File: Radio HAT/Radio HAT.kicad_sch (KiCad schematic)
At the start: 21 parts, among them J1 Raspberry_Pi_2_3, J2 Coax SMA, J3 Barrel_Jack, J4 VCC, J5 6V, J6 GND, U1 RFM98PW, U2 AZ2185D-ADJTRG1

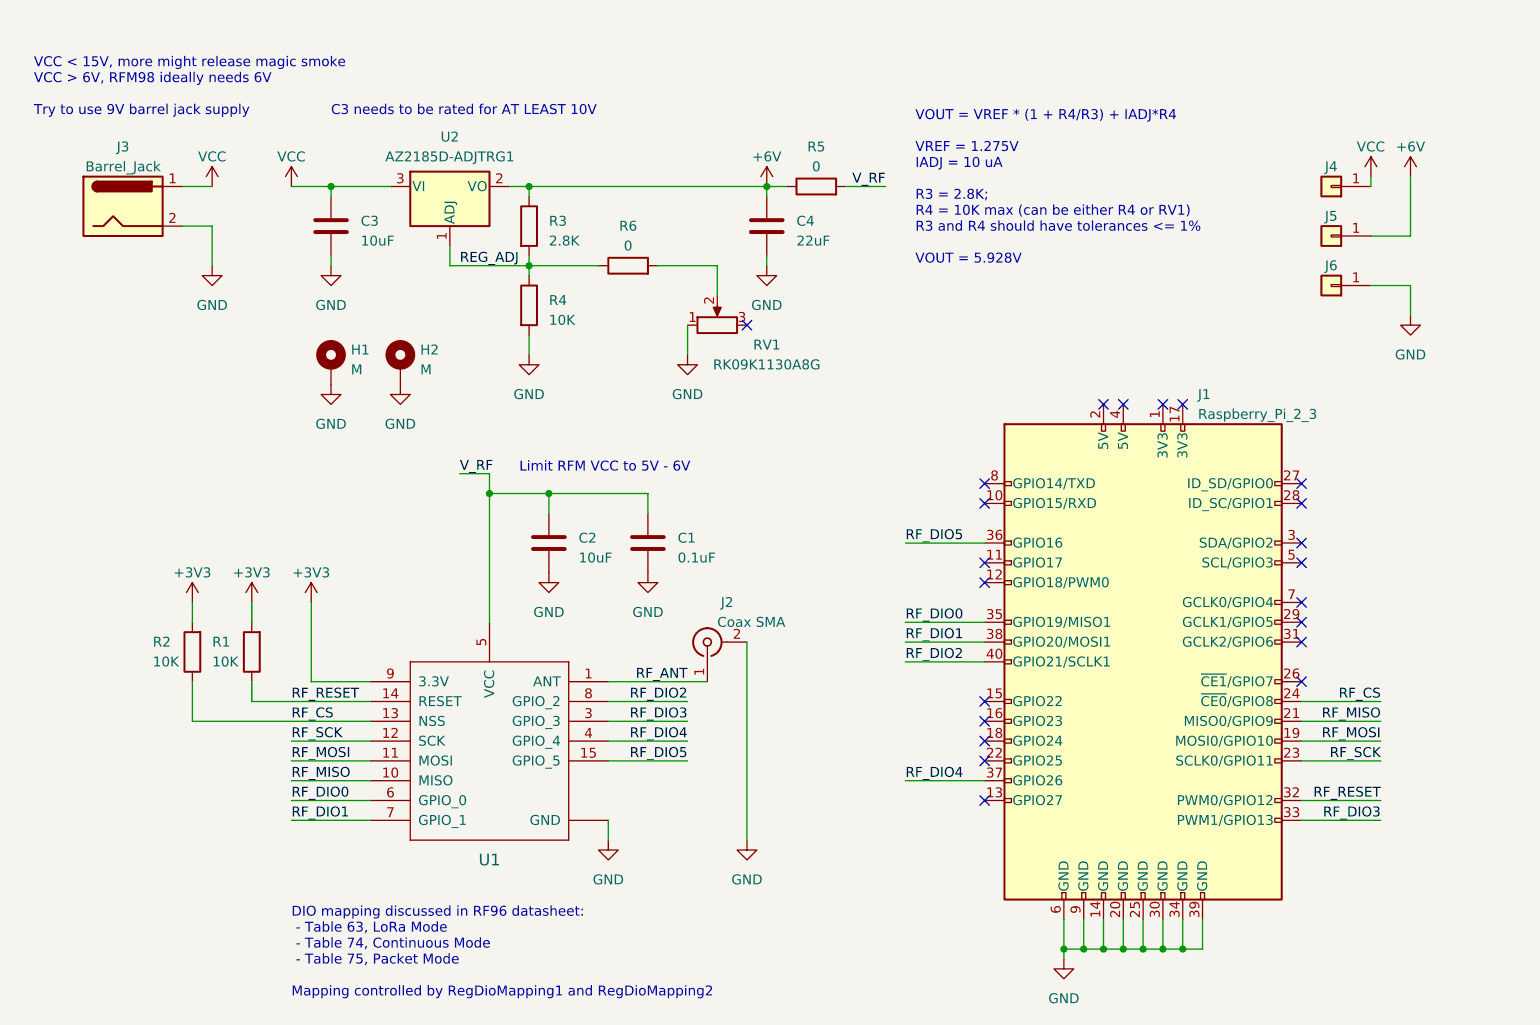
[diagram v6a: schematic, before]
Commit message: Updated schematic, changed power routing
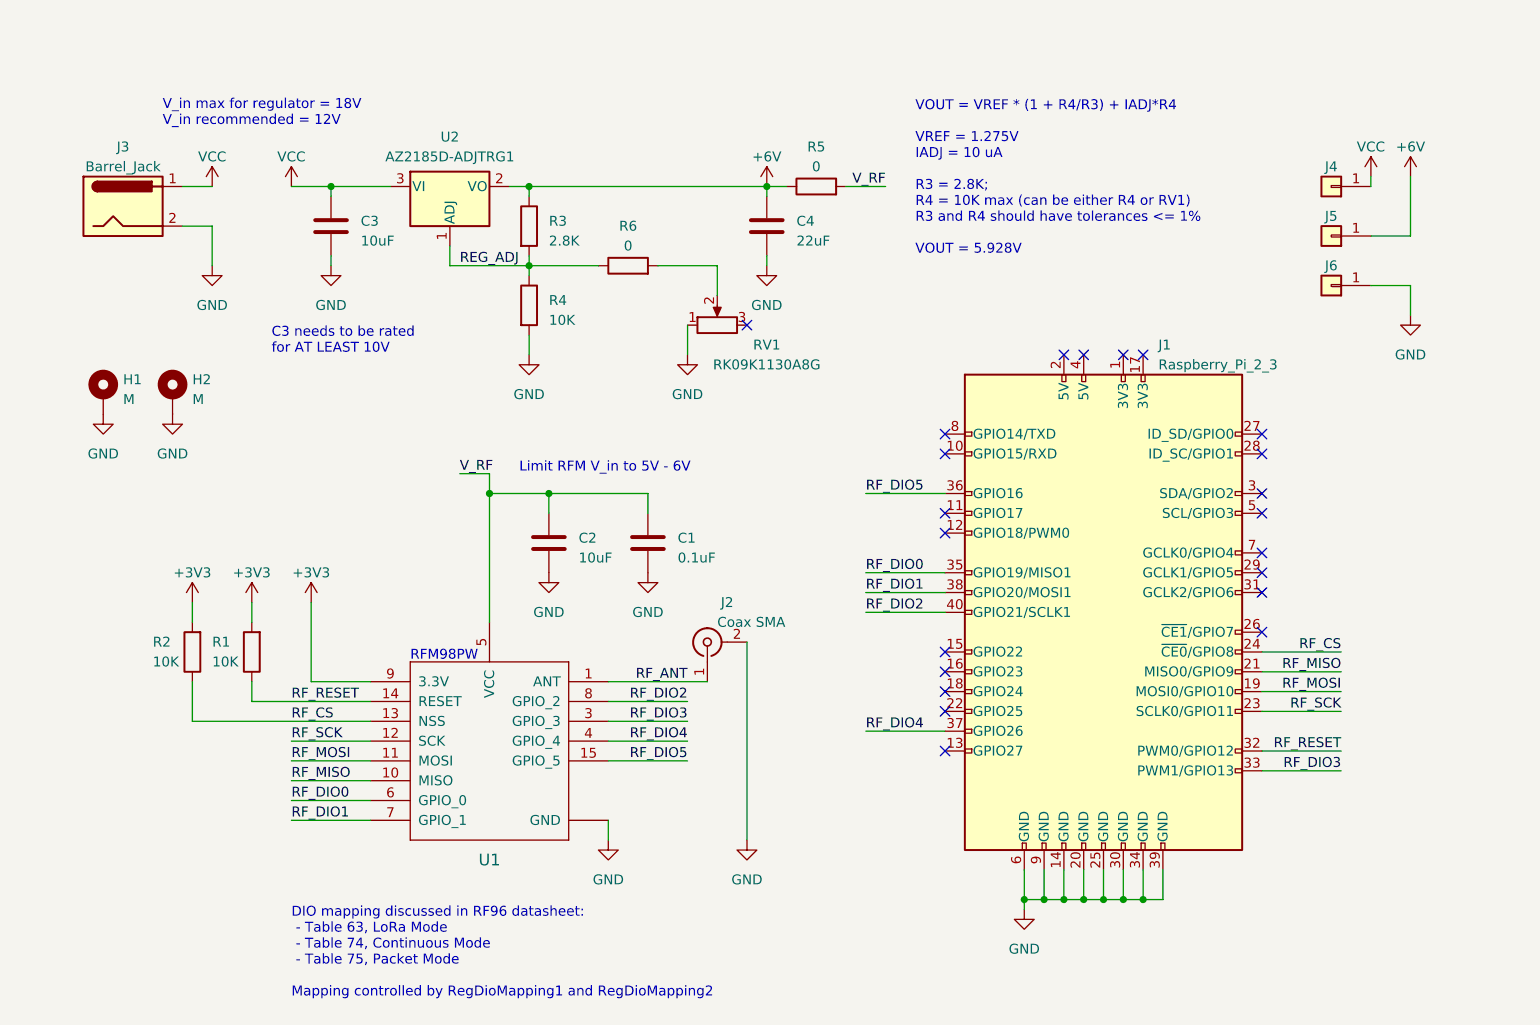
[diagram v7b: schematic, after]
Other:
- note added: "Limit RFM V_in to 5V - 6V"
- note added: "RFM98PW"
- note added: "V_in max for regulator = 18V V_in recommended = 12V"
- note removed: "Limit RFM VCC to 5V - 6V"
- note removed: "VCC < 15V, more might release magic smoke VCC > 6V, RFM98 ideally needs 6V Try to use 9V barrel jack supply"
- moved on the sheet: H1, H2, J1

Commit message: Reworked power traces, added stitching vias
Reworked 3V3 net, added stitching vias on board, added passive components, regenerated BOM and STEP file for board
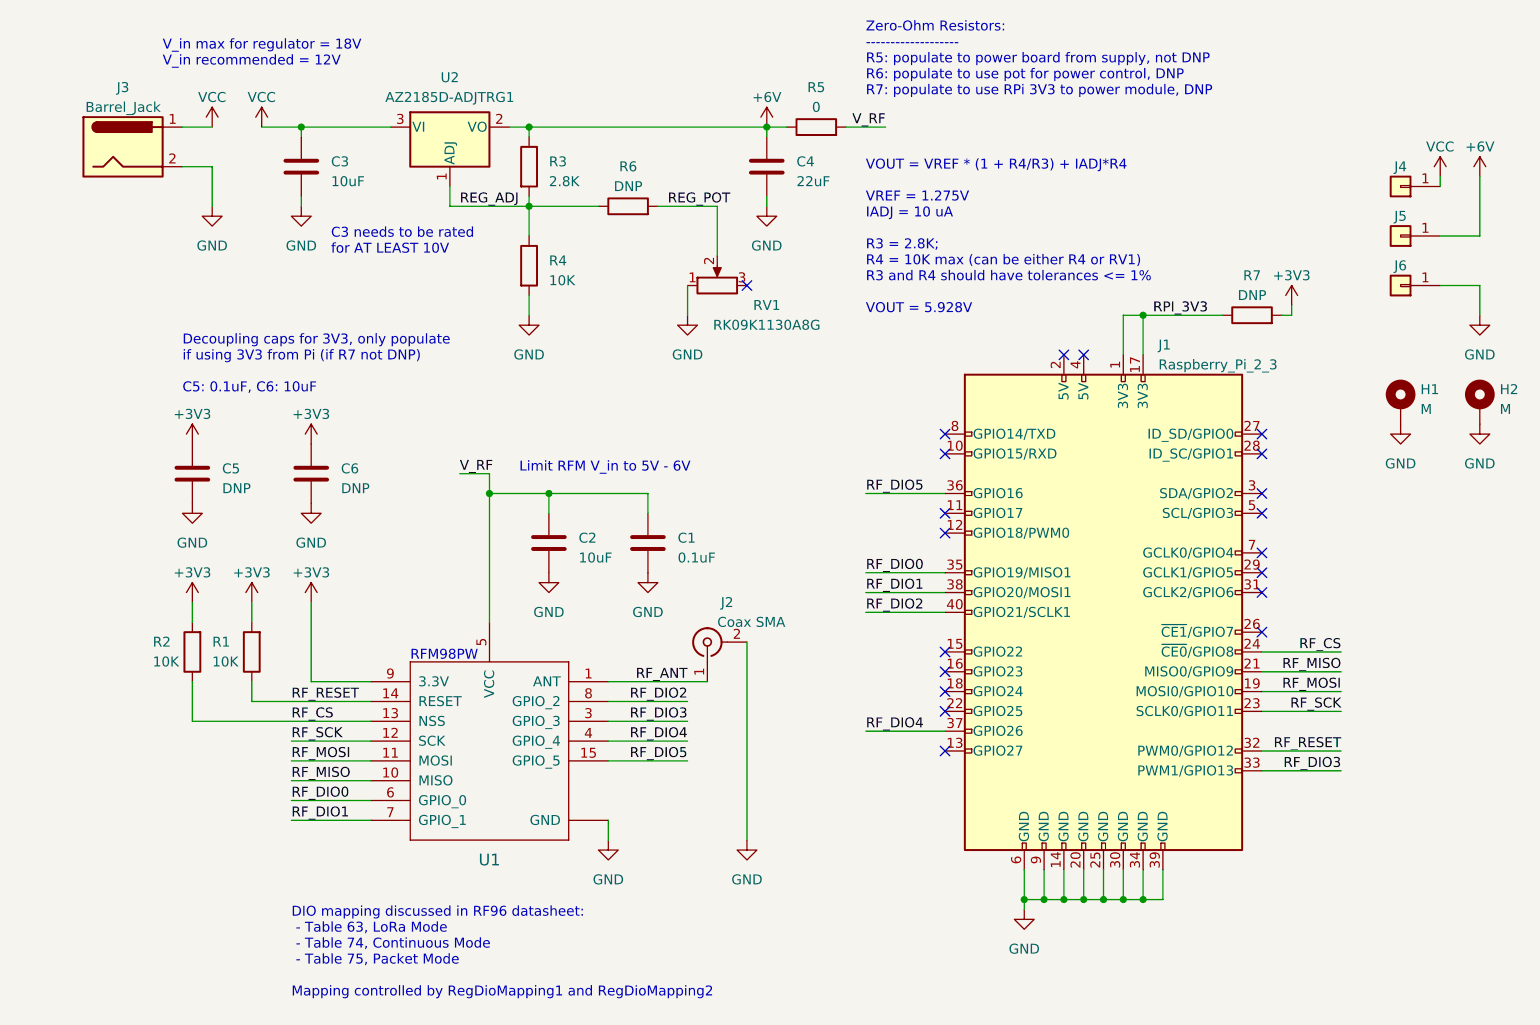
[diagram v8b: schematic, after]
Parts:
- added C5, C6: DNP, Capacitor_SMD:C_0603_1608Metric_Pad1.08x0.95mm_HandSolder, symbol Device:C
- added R7: DNP, Resistor_SMD:R_0805_2012Metric_Pad1.20x1.40mm_HandSolder, symbol Device:R
- R6: value 0 -> DNP
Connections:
- net +3V3: now also C5.1, C6.1, R7.2
- net GND: now also C5.2, C6.2
- net REG_POT: now reaches R6.2, RV1.2
- net RPI_3V3: now reaches J1.1 (3V3)
- net RPI_3V3: now also J1.17 (3V3), R7.1
- no-connect marks 22 -> 20
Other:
- note added: "Decoupling caps for 3V3, only populate if using 3V3 from Pi (if R7 not DNP) C5: 0.1uF, C6: 10uF"
- note added: "Zero-Ohm Resistors: ------------------- R5: populate to power board from supply, not DNP R6: populate to use pot for power control, DNP R7: populate to use RPi 3V3 to power module, DNP"
- moved on the sheet: C3, C4, H1, H2, J3, J4, J5, J6, R3, R4, R5, R6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
